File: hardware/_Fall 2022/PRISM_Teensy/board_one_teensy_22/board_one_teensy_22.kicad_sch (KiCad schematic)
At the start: 15 parts, among them J1 EAST, J2 CORE_IO, J3 USB_micro, U1 Teensy4.1, U2 BNO055_Breakout, U3 3966

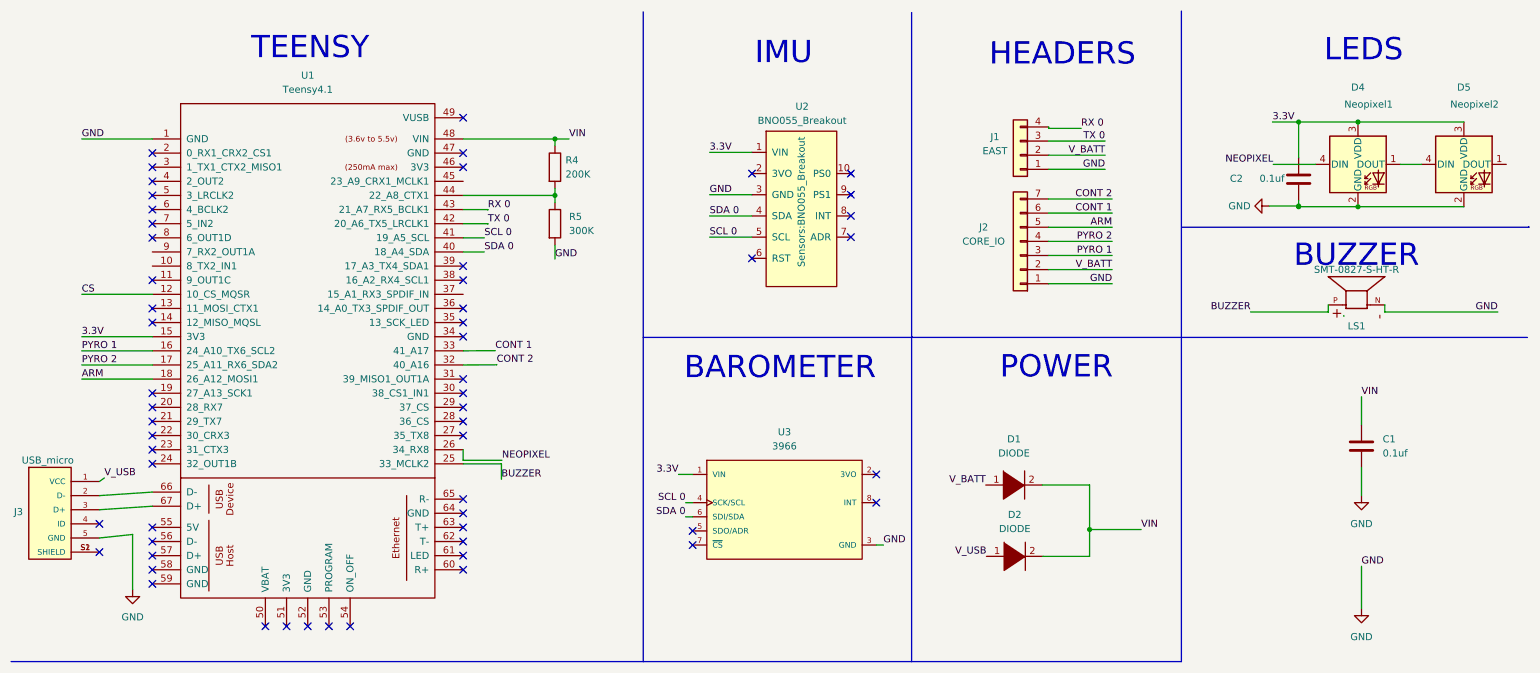
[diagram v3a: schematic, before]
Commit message: Add schottcky diodes to main teensy
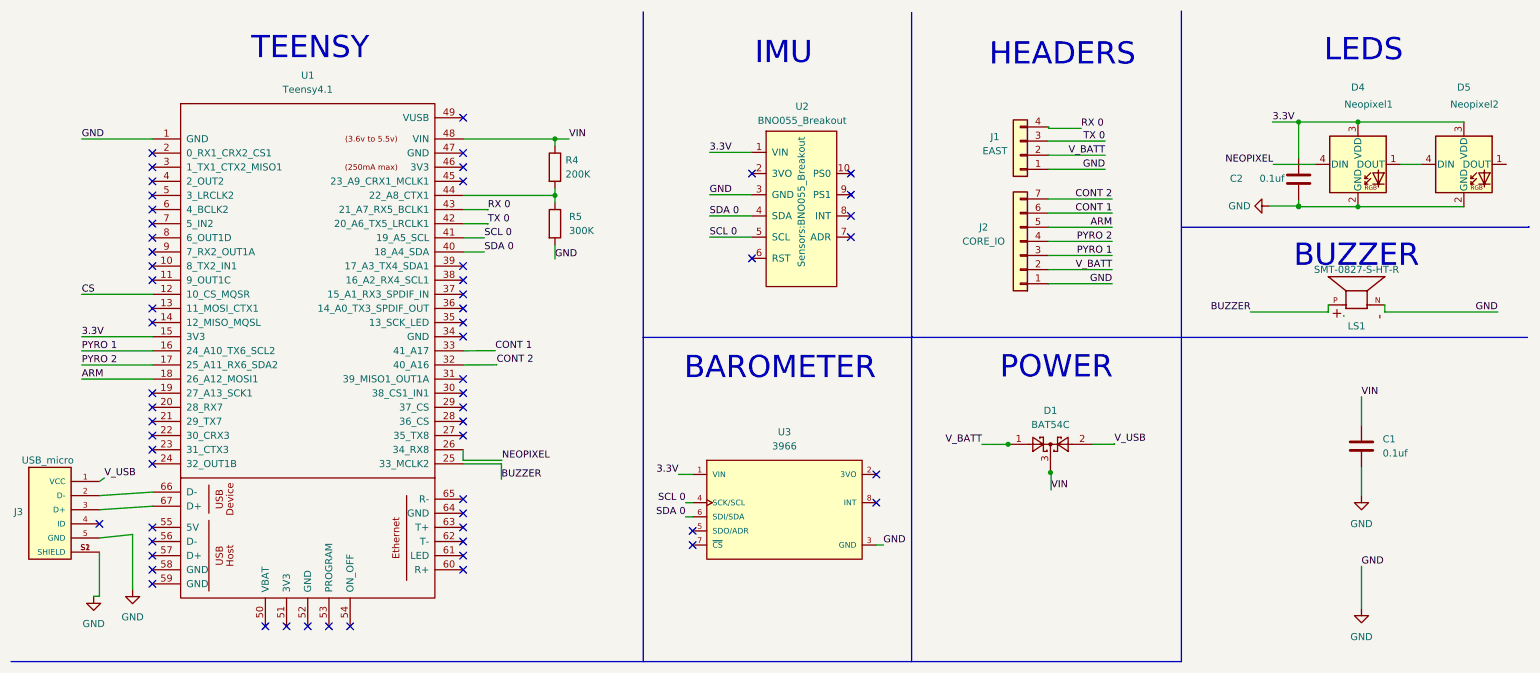
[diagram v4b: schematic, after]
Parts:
- removed D1, D2: DIODE, Diode_SMD:D_0201_0603Metric, symbol pspice:DIODE
- added D1: BAT54C, Package_TO_SOT_SMD:SOT-23, symbol Diode:BAT54C
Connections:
- net GND: now also J3.S1 (SHIELD), J3.S2 (SHIELD)
- net VIN: now also D1.3
- net V_BATT: now also D1.1
- net V_USB: now also D1.2
- no-connect marks 57 -> 60
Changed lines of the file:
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@@
   (junction (at 243.586 47.117) (diameter 0) (color 0 0 0 0)
   )
-  (junction (at 205.994 105.156) (diameter 0) (color 0 0 0 0)
-  )
   (junction (at 254.254 31.877) (diameter 0) (color 0 0 0 0)
   )
   (junction (at 109.855 34.925) (diameter 0) (color 0 0 0 0)
   )
+  (junction (at 191.3408 89.8332) (diameter 0) (color 0 0 0 0)
+  )
   (junction (at 243.586 46.99) (diameter 0) (color 0 0 0 0)
   )
@@
   (junction (at 243.586 31.877) (diameter 0) (color 0 0 0 0)
   )
+  (junction (at 198.9608 94.9132) (diameter 0) (color 0 0 0 0)
+  )
+  (no_connect (at 37.465 55.245))
+  (no_connect (at 37.465 57.785))
+  (no_connect (at 93.345 42.545))
+  (no_connect (at 93.345 62.865))
   (no_connect (at 37.465 90.805))
   (no_connect (at 37.465 80.645))
   (no_connect (at 163.068 44.958))
   (no_connect (at 27.94 104.14))
-  (no_connect (at 27.94 109.22))
   (no_connect (at 93.345 40.005))
   (no_connect (at 93.345 37.465))
@@
     (stroke (width 0) (type default) (color 0 0 0 0))
   )
+  (wire (pts (xy 206.5808 89.8332) (xy 210.4614 89.8332))
+    (stroke (width 0) (type default) (color 0 0 0 0))
+  )
   (wire (pts (xy 210.058 55.88) (xy 198.628 55.88))
     (stroke (width 0) (type default) (color 0 0 0 0))
@@
     (stroke (width 0) (type default) (color 0 0 0 0))
   )
+  (wire (pts (xy 199.0862 98.051) (xy 199.0862 94.9132))
+    (stroke (width 0) (type default) (color 0 0 0 0))
+  )
   (wire (pts (xy 210.058 48.26) (xy 198.628 48.26))
     (stroke (width 0) (type default) (color 0 0 0 0))
@@
     (stroke (width 0) (type default) (color 0 0 0 0))
   )
+  (wire (pts (xy 199.0862 94.9132) (xy 198.9608 94.9132))
+    (stroke (width 0) (type default) (color 0 0 0 0))
+  )
   (wire (pts (xy 198.628 33.02) (xy 198.628 32.766))
     (stroke (width 0) (type default) (color 0 0 0 0))
   )
+  (wire (pts (xy 186.6541 89.8468) (xy 191.3408 89.8468))
+    (stroke (width 0) (type default) (color 0 0 0 0))
+  )
   (polyline (pts (xy 12.065 128.905) (xy 125.73 128.905))
     (stroke (width 0) (type default) (color 0 0 0 0))
@@
     (stroke (width 0) (type default) (color 0 0 0 0))
   )
-  (wire (pts (xy 197.485 97.155) (xy 205.994 97.155))
+  (wire (pts (xy 27.94 117.1566) (xy 26.9042 117.1566))
     (stroke (width 0) (type default) (color 0 0 0 0))
   )
@@
     (stroke (width 0) (type default) (color 0 0 0 0))
   )
+  (wire (pts (xy 210.4614 89.8332) (xy 210.4614 89.6958))
+    (stroke (width 0) (type default) (color 0 0 0 0))
+  )
   (wire (pts (xy 243.586 31.877) (xy 254.254 31.877))
     (stroke (width 0) (type default) (color 0 0 0 0))
@@
     (stroke (width 0) (type default) (color 0 0 0 0))
   )
-  (wire (pts (xy 205.994 109.982) (xy 205.994 105.156))
-    (stroke (width 0) (type default) (color 0 0 0 0))
-  )
   (wire (pts (xy 243.586 45.974) (xy 243.586 46.99))
     (stroke (width 0) (type default) (color 0 0 0 0))
@@
     (stroke (width 0) (type default) (color 0 0 0 0))
   )
-  (wire (pts (xy 197.612 109.982) (xy 205.994 109.982))
-    (stroke (width 0) (type default) (color 0 0 0 0))
-  )
   (wire (pts (xy 133.35 102.87) (xy 134.62 102.87))
     (stroke (width 0) (type default) (color 0 0 0 0))
@@
     (stroke (width 0) (type default) (color 0 0 0 0))
   )
+  (wire (pts (xy 27.94 109.22) (xy 27.94 117.1566))
+    (stroke (width 0) (type default) (color 0 0 0 0))
+  )
   (wire (pts (xy 248.92 66.04) (xy 248.92 64.77))
     (stroke (width 0) (type default) (color 0 0 0 0))
   )
-  (wire (pts (xy 205.994 97.155) (xy 205.994 105.156))
-    (stroke (width 0) (type default) (color 0 0 0 0))
-  )
   (wire (pts (xy 97.7931 50.165) (xy 97.7931 50.2346))
     (stroke (width 0) (type default) (color 0 0 0 0))
@@
     (stroke (width 0) (type default) (color 0 0 0 0))
   )
-  (wire (pts (xy 205.994 105.156) (xy 215.265 105.156))
-    (stroke (width 0) (type default) (color 0 0 0 0))
-  )
   (wire (pts (xy 93.345 34.925) (xy 109.855 34.925))
     (stroke (width 0) (type default) (color 0 0 0 0))
@@
   )
   (wire (pts (xy 279.4 66.04) (xy 259.08 66.04))
+    (stroke (width 0) (type default) (color 0 0 0 0))
+  )
+  (wire (pts (xy 191.3408 89.8468) (xy 191.3408 89.8332))
     (stroke (width 0) (type default) (color 0 0 0 0))
   )
@@
     (effects (font (size 1.27 1.27)) (justify right bottom))
   )
-  (label "VIN" (at 215.265 105.156 0)
+  (label "VIN" (at 199.0862 98.051 0)
     (effects (font (size 1.27 1.27)) (justify left bottom))
   )
@@
     (effects (font (size 1.27 1.27)) (justify left bottom))
   )
-  (label "V_USB" (at 187.452 109.982 180)
-    (effects (font (size 1.27 1.27)) (justify right bottom))
+  (label "V_USB" (at 210.4614 89.6958 0)
+    (effects (font (size 1.27 1.27)) (justify left bottom))
   )
   (label "V_USB" (at 28.829 95.885 0)
@@
     (effects (font (size 1.27 1.27)) (justify left bottom))
   )
-  (label "V_BATT" (at 187.325 97.155 180)
+  (label "V_BATT" (at 186.6541 89.8468 180)
     (effects (font (size 1.27 1.27)) (justify right bottom))
   )
@@
   (label "V_BATT" (at 208.788 37.846 180)
     (effects (font (size 1.27 1.27)) (justify right bottom))
+  )
+  (symbol (lib_id "Diode:BAT54C") (at 198.9608 89.8332 0) (unit 1)
+    (in_bom yes) (on_board yes) (fields_autoplaced)
+    (property "Reference" "D1" (id 0) (at 198.9608 83.7719 0))
+    (property "Value" "BAT54C" (id 1) (at 198.9608 86.3119 0))
+    (property "Footprint" "Package_TO_SOT_SMD:SOT-23" (id 2) (at 200.8658 86.6582 0)
+      (effects (font (size 1.27 1.27)) (justify left) hide)
+    )
+    (property "Datasheet" "http://www.diodes.com/_files/datasheets/ds11005.pdf" (id 3) (at 196.9288 89.8332 0)
+      (effects (font (size 1.27 1.27)) hide)
+    )
+    (property "JLC" "C369922" (id 4) (at 198.9608 89.8332 0)
+      (effects (font (size 1.27 1.27)) hide)
+    )
+    (pin "1")
+    (pin "2")
+    (pin "3")
   )
   (symbol (lib_id "LED:NeoPixel_THT") (at 273.304 39.497 0) (unit 1)
@@
     (pin "2")
   )
+  (symbol (lib_id "power:GND") (at 26.9042 117.1566 0) (unit 1)
+    (in_bom yes) (on_board yes) (fields_autoplaced)
+    (property "Reference" "#PWR0102" (id 0) (at 26.9042 123.5066 0)
+      (effects (font (size 1.27 1.27)) hide)
+    )
+    (property "Value" "GND" (id 1) (at 26.9042 122.1096 0))
+    (property "Footprint" "" (id 2) (at 26.9042 117.1566 0)
+      (effects (font (size 1.27 1.27)) hide)
+    )
+    (property "Datasheet" "" (id 3) (at 26.9042 117.1566 0)
+      (effects (font (size 1.27 1.27)) hide)
+    )
+    (pin "1")
+  )
   (symbol (lib_id "Device:R") (at 109.855 40.005 0) (unit 1)
     (in_bom yes) (on_board yes) (fields_autoplaced)
@@
     )
     (pin "1")
-  )
-  (symbol (lib_id "pspice:DIODE") (at 192.532 109.982 0) (unit 1)
-    (in_bom yes) (on_board yes) (fields_autoplaced)
-    (property "Reference" "D2" (id 0) (at 192.532 102.489 0))
-    (property "Value" "DIODE" (id 1) (at 192.532 105.029 0))
-    (property "Footprint" "Diode_SMD:D_0201_0603Metric" (id 2) (at 192.532 109.982 0)
-      (effects (font (size 1.27 1.27)) hide)
-    )
-    (property "Datasheet" "~" (id 3) (at 192.532 109.982 0)
-      (effects (font (size 1.27 1.27)) hide)
-    )
-    (pin "1")
-    (pin "2")
   )
   (symbol (lib_id "Connector_Generic:Conn_01x04") (at 193.548 37.846 180) (unit 1)
@@
     )
     (pin "1")
-  )
-  (symbol (lib_id "pspice:DIODE") (at 192.405 97.155 0) (unit 1)
-    (in_bom yes) (on_board yes) (fields_autoplaced)
-    (property "Reference" "D1" (id 0) (at 192.405 88.9 0))
-    (property "Value" "DIODE" (id 1) (at 192.405 91.44 0))
-    (property "Footprint" "Diode_SMD:D_0201_0603Metric" (id 2) (at 192.405 97.155 0)
-      (effects (font (size 1.27 1.27)) hide)
-    )
-    (property "Datasheet" "~" (id 3) (at 192.405 97.155 0)
-      (effects (font (size 1.27 1.27)) hide)
-    )
-    (pin "1")
-    (pin "2")
   )
   (symbol (lib_id "Teensy:Teensy4.1") (at 65.405 89.535 0) (unit 1)
@@
       (reference "#PWR0101") (unit 1) (value "GND") (footprint "")
     )
+    (path "/8f848182-f8f2-4efc-a420-ecd77eeaa049"
+      (reference "#PWR0102") (unit 1) (value "GND") (footprint "")
+    )
     (path "/ed2d98ad-ef42-4a14-aff6-3752d42a2ad5"
       (reference "C1") (unit 1) (value "0.1uf") (footprint "Capacitor_SMD:C_0201_0603Metric")
@@
       (reference "C2") (unit 1) (value "0.1uf") (footprint "Capacitor_SMD:C_0201_0603Metric")
     )
-    (path "/fed88b2e-3769-4111-82b6-285fe17003ad"
-      (reference "D1") (unit 1) (value "DIODE") (footprint "Diode_SMD:D_0201_0603Metric")
-    )
-    (path "/bb3c97a3-e89e-41ec-af24-736a68f2b9c3"
-      (reference "D2") (unit 1) (value "DIODE") (footprint "Diode_SMD:D_0201_0603Metric")
+    (path "/584fd14d-2b31-477f-8140-fcd6e0991dda"
+      (reference "D1") (unit 1) (value "BAT54C") (footprint "Package_TO_SOT_SMD:SOT-23")
     )
     (path "/a2dee755-f29c-470f-8c5e-e23ef91a94a4"
